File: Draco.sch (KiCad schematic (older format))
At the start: 50 parts, among them J1 Conn_01x03, J10 Conn_01x03, J11 Conn_01x06, J12 Conn_02x05_Odd_Even, J13 Conn_01x04, J14 Conn_01x01, J15 Micro_SD_Card, J2 Conn_01x03, J3 Conn_01x03, J4 Conn_01x03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

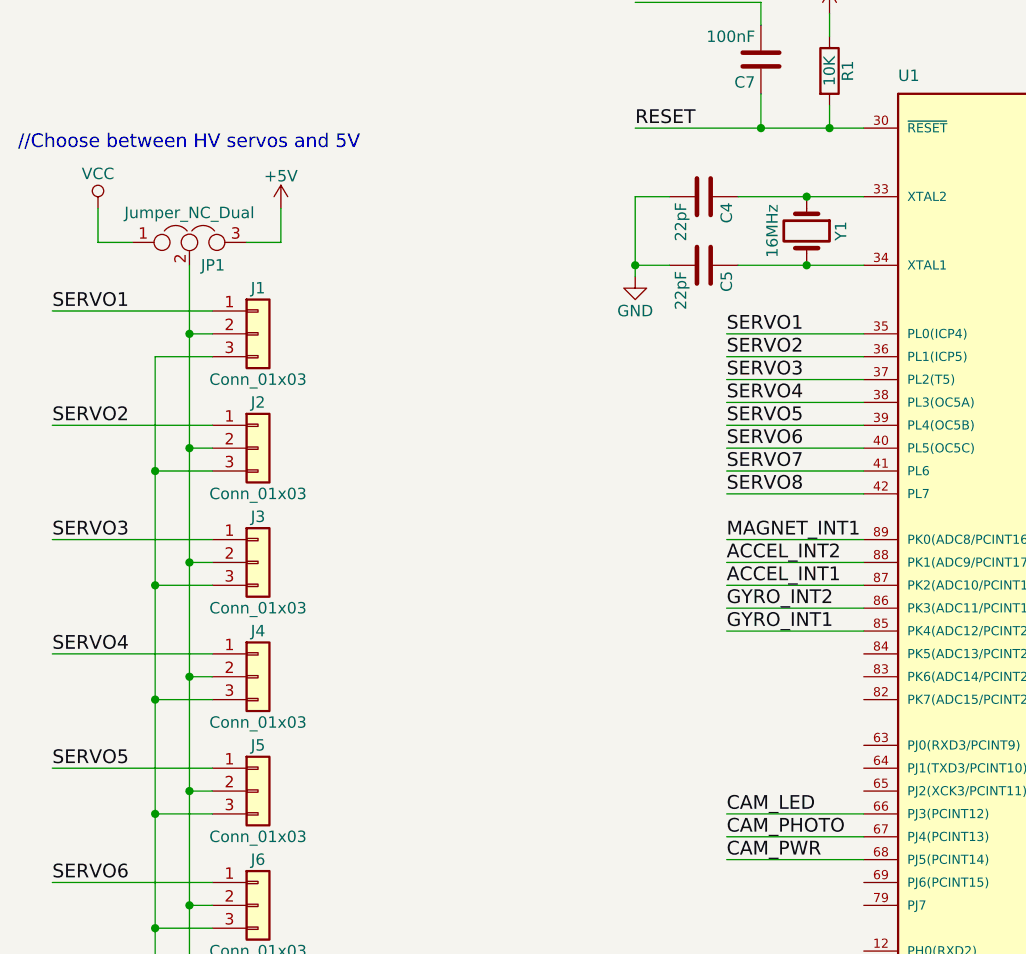
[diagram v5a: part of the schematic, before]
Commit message: moved charge module, routed lots of stuff
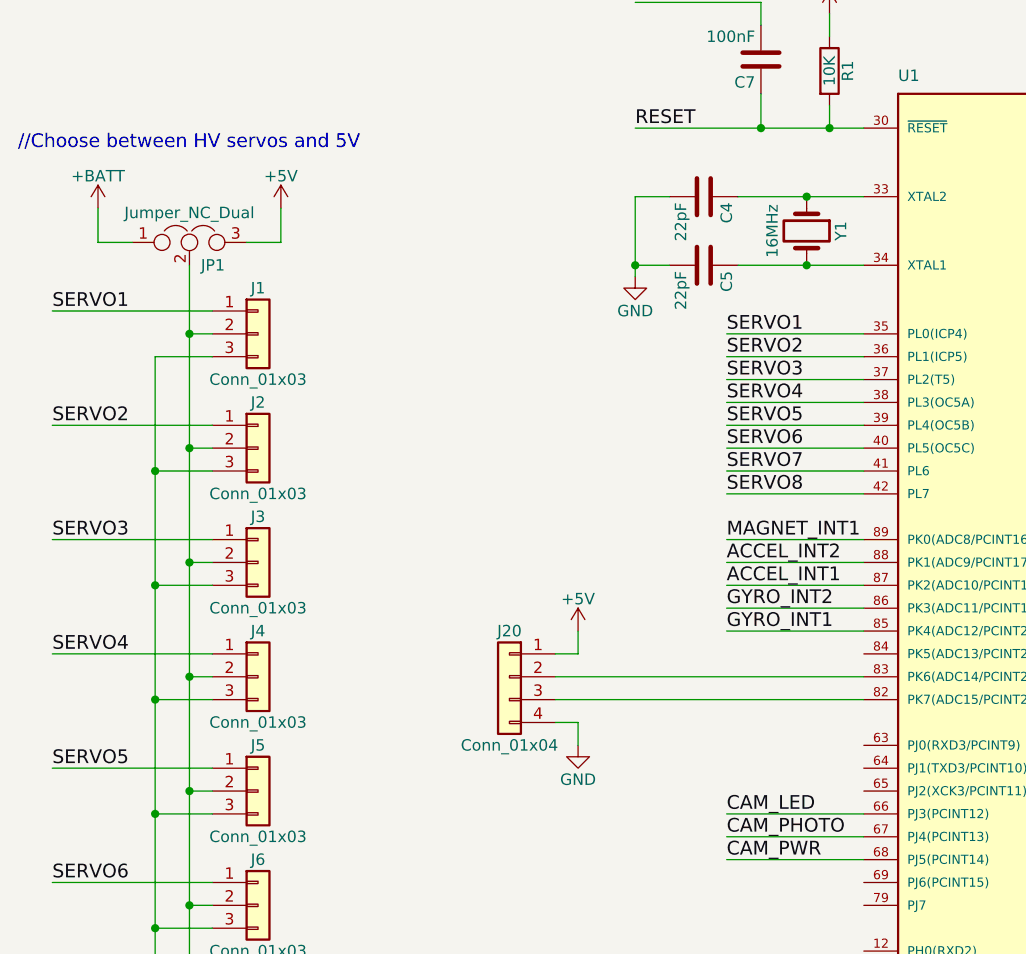
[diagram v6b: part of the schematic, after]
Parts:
- added J20: Conn_01x04, Pin_Headers:Pin_Header_Angled_1x04_Pitch2.54mm, symbol Conn_01x04
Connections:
- net VCC is gone; now on net +BATT: JP1.1
- net +5V: now also J20.1 (Pin_1)
- net GND: now also J20.4 (Pin_4)
- net at U1.82 (PK7(ADC15/PCINT23)): now also J20.3 (Pin_3)
- net at U1.83 (PK6(ADC14/PCINT22)): now also J20.2 (Pin_2)
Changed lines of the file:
@@
 LIBS:TXB0104DR
 LIBS:LOGIC-TXS0108EPWR_TSSOP20_
-LIBS:CurrentControlSystems
 LIBS:Draco-cache
 EELAYER 25 0
@@
 Text Notes 11000 4800 0    60   ~ 0
 CAM_PWR needs 9.8k-3.13k
-$Comp
-L VCC #PWR030
-U 1 1 5A686F0B
-P 1450 2550
-F 0 "#PWR030" H 1450 2400 50  0001 C CNN
-F 1 "VCC" H 1450 2700 50  0000 C CNN
-F 2 "" H 1450 2550 50  0001 C CNN
-F 3 "" H 1450 2550 50  0001 C CNN
-	1    1450 2550
-	1    0    0    -1
-$EndComp
 Wire Wire Line
 	4800 6100 4200 6100
@@
 Text Label 8050 7100 2    60   ~ 0
 VBAT2
+$Comp
+L Conn_01x04 J20
+U 1 1 5A6A227C
+P 3250 4600
+F 0 "J20" H 3250 4800 50  0000 C CNN
+F 1 "Conn_01x04" H 3250 4300 50  0000 C CNN
+F 2 "Pin_Headers:Pin_Header_Angled_1x04_Pitch2.54mm" H 3250 4600 50  0001 C CNN
+F 3 "" H 3250 4600 50  0001 C CNN
+	1    3250 4600
+	-1   0    0    -1
+$EndComp
+Wire Wire Line
+	4800 4600 3450 4600
+Wire Wire Line
+	4800 4700 3450 4700
+Wire Wire Line
+	3450 4500 3550 4500
+Wire Wire Line
+	3550 4500 3550 4400
+Wire Wire Line
+	3450 4800 3550 4800
+Wire Wire Line
+	3550 4800 3550 4900
+$Comp
+L GND #PWR034
+U 1 1 5A6A2B9C
+P 3550 4900
+F 0 "#PWR034" H 3550 4650 50  0001 C CNN
+F 1 "GND" H 3550 4750 50  0000 C CNN
+F 2 "" H 3550 4900 50  0001 C CNN
+F 3 "" H 3550 4900 50  0001 C CNN
+	1    3550 4900
+	1    0    0    -1
+$EndComp
+$Comp
+L +5V #PWR035
+U 1 1 5A6A2F82
+P 3550 4400
+F 0 "#PWR035" H 3550 4250 50  0001 C CNN
+F 1 "+5V" H 3550 4540 50  0000 C CNN
+F 2 "" H 3550 4400 50  0001 C CNN
+F 3 "" H 3550 4400 50  0001 C CNN
+	1    3550 4400
+	1    0    0    -1
+$EndComp
+$Comp
+L +BATT #PWR?
+U 1 1 5A6A6502
+P 1450 2550
+F 0 "#PWR?" H 1450 2400 50  0001 C CNN
+F 1 "+BATT" H 1450 2690 50  0000 C CNN
+F 2 "" H 1450 2550 50  0001 C CNN
+F 3 "" H 1450 2550 50  0001 C CNN
+	1    1450 2550
+	1    0    0    -1
+$EndComp
 $EndSCHEMATC

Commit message: Routed 50%
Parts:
- J20: footprint Pin_Headers:Pin_Header_Angled_1x04_Pitch2.54mm -> Connectors_JST:JST_XH_B04B-XH-A_04x2.50mm_Straight
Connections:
- net 3V_LORA_NSS: now also U2.6 (A5); no longer U2.7 (A6)
- net 3V_LORA_RST: now also U2.5 (A4); no longer U2.9 (A8)
- net 3V_MISO: now also U2.9 (A8); no longer U2.5 (A4)
- net 3V_MOSI: now also U2.8 (A7); no longer U2.4 (A3)
- net 3V_SCK: now also U2.7 (A6); no longer U2.6 (A5)
- net 3V_SD_NSS: now also U2.4 (A3); no longer U2.8 (A7)
- net 5V_LORA_NSS: now also U2.15 (B5); no longer U2.14 (B6)
- net 5V_LORA_RST: now also U2.16 (B4); no longer U2.12 (B8)
- net 5V_MISO: now also U2.12 (B8); no longer U2.16 (B4)
- net 5V_MOSI: now also U2.13 (B7); no longer U2.17 (B3)
- net 5V_SCK: now also U2.14 (B6); no longer U2.15 (B5)
- net 5V_SD_NSS: now also U2.17 (B3); no longer U2.13 (B7)
- net CAM_PHOTO: now also R10.2; no longer R11.2
- net CAM_PWR: now also R11.2; no longer R10.2
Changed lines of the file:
@@
 LIBS:TXB0104DR
 LIBS:LOGIC-TXS0108EPWR_TSSOP20_
+LIBS:CurrentControlSystems
 LIBS:Draco-cache
 EELAYER 25 0
@@
 Text Label 10900 7700 0    60   ~ 0
 3V_SDA
-Text Label 13100 7800 2    60   ~ 0
+Text Label 13100 8200 2    60   ~ 0
 5V_MOSI
-Text Label 13100 7900 2    60   ~ 0
+Text Label 13100 8300 2    60   ~ 0
 5V_MISO
+Text Label 13100 8100 2    60   ~ 0
+5V_SCK
+Text Label 10900 8200 0    60   ~ 0
+3V_MOSI
+Text Label 10900 8300 0    60   ~ 0
+3V_MISO
+Text Label 10900 8100 0    60   ~ 0
+3V_SCK
 Text Label 13100 8000 2    60   ~ 0
-5V_SCK
-Text Label 10900 7800 0    60   ~ 0
-3V_MOSI
-Text Label 10900 7900 0    60   ~ 0
-3V_MISO
+5V_LORA_NSS
 Text Label 10900 8000 0    60   ~ 0
-3V_SCK
-Text Label 13100 8100 2    60   ~ 0
-5V_LORA_NSS
-Text Label 10900 8100 0    60   ~ 0
 3V_LORA_NSS
 Text Label 13650 7650 0    60   ~ 0
@@
 Text Label 12700 4950 0    60   ~ 0
 3V_SD_NSS
-Text Label 10900 8200 0    60   ~ 0
+Text Label 10900 7800 0    60   ~ 0
 3V_SD_NSS
-Text Label 13100 8200 2    60   ~ 0
+Text Label 13100 7800 2    60   ~ 0
 5V_SD_NSS
 Text Label 8050 2900 2    60   ~ 0
@@
 Text Label 13650 8150 0    60   ~ 0
 3V_LORA_RST
-Text Label 10900 8300 0    60   ~ 0
+Text Label 10900 7900 0    60   ~ 0
 3V_LORA_RST
-Text Label 13100 8300 2    60   ~ 0
+Text Label 13100 7900 2    60   ~ 0
 5V_LORA_RST
 Text Label 8050 6200 2    60   ~ 0
@@
 	11500 7700 10900 7700
 Wire Wire Line
+	12400 8200 13100 8200
+Wire Wire Line
+	12400 8300 13100 8300
+Wire Wire Line
+	12400 8100 13100 8100
+Wire Wire Line
+	11500 8200 10900 8200
+Wire Wire Line
+	11500 8300 10900 8300
+Wire Wire Line
+	11500 8100 10900 8100
+Wire Wire Line
+	12400 8000 13100 8000
+Wire Wire Line
+	11500 8000 10900 8000
+Wire Wire Line
+	14600 7650 13650 7650
+Wire Wire Line
+	14600 7750 13650 7750
+Wire Wire Line
+	14600 7850 13650 7850
+Wire Wire Line
+	14600 7950 13650 7950
+Wire Wire Line
+	13650 2150 12950 2150
+Wire Wire Line
+	13650 2300 12950 2300
+Wire Wire Line
+	13350 5150 13800 5150
+Wire Wire Line
+	13700 5150 13700 4500
+Wire Wire Line
+	13800 5350 13700 5350
+Wire Wire Line
+	13700 5350 13700 5850
+Wire Wire Line
+	13800 5250 12700 5250
+Wire Wire Line
+	13800 5450 12700 5450
+Wire Wire Line
+	13800 5050 12700 5050
+Wire Wire Line
+	13800 4950 12700 4950
+Wire Wire Line
+	11500 7800 10900 7800
+Wire Wire Line
 	12400 7800 13100 7800
 Wire Wire Line
+	7400 2900 8050 2900
+Wire Wire Line
+	4800 3100 4200 3100
+Wire Wire Line
+	4800 3200 4200 3200
+Wire Wire Line
+	4800 3300 4200 3300
+Wire Wire Line
+	4800 3400 4200 3400
+Wire Wire Line
+	4800 3500 4200 3500
+Wire Wire Line
+	4800 3600 4200 3600
+Wire Wire Line
+	4800 3700 4200 3700
+Wire Wire Line
+	4800 3800 4200 3800
+Wire Wire Line
+	7400 6500 8050 6500
+Wire Wire Line
+	7400 6400 8050 6400
+Wire Wire Line
+	11500 7500 11400 7500
+Wire Wire Line
+	11400 7500 11400 7250
+Wire Wire Line
+	15700 7600 16200 7600
+Wire Wire Line
+	14600 8150 13650 8150
+Wire Wire Line
+	11500 7900 10900 7900
+Wire Wire Line
 	12400 7900 13100 7900
-Wire Wire Line
-	12400 8000 13100 8000
-Wire Wire Line
-	11500 7800 10900 7800
-Wire Wire Line
-	11500 7900 10900 7900
-Wire Wire Line
-	11500 8000 10900 8000
-Wire Wire Line
-	12400 8100 13100 8100
-Wire Wire Line
-	11500 8100 10900 8100
-Wire Wire Line
-	14600 7650 13650 7650
-Wire Wire Line
-	14600 7750 13650 7750
-Wire Wire Line
-	14600 7850 13650 7850
-Wire Wire Line
-	14600 7950 13650 7950
-Wire Wire Line
-	13650 2150 12950 2150
-Wire Wire Line
-	13650 2300 12950 2300
-Wire Wire Line
-	13350 5150 13800 5150
-Wire Wire Line
-	13700 5150 13700 4500
-Wire Wire Line
-	13800 5350 13700 5350
-Wire Wire Line
-	13700 5350 13700 5850
-Wire Wire Line
-	13800 5250 12700 5250
-Wire Wire Line
-	13800 5450 12700 5450
-Wire Wire Line
-	13800 5050 12700 5050
-Wire Wire Line
-	13800 4950 12700 4950
-Wire Wire Line
-	11500 8200 10900 8200
-Wire Wire Line
-	12400 8200 13100 8200
-Wire Wire Line
-	7400 2900 8050 2900
-Wire Wire Line
-	4800 3100 4200 3100
-Wire Wire Line
-	4800 3200 4200 3200
-Wire Wire Line
-	4800 3300 4200 3300
-Wire Wire Line
-	4800 3400 4200 3400
-Wire Wire Line
-	4800 3500 4200 3500
-Wire Wire Line
-	4800 3600 4200 3600
-Wire Wire Line
-	4800 3700 4200 3700
-Wire Wire Line
-	4800 3800 4200 3800
-Wire Wire Line
-	7400 6500 8050 6500
-Wire Wire Line
-	7400 6400 8050 6400
-Wire Wire Line
-	11500 7500 11400 7500
-Wire Wire Line
-	11400 7500 11400 7250
-Wire Wire Line
-	15700 7600 16200 7600
-Wire Wire Line
-	14600 8150 13650 8150
-Wire Wire Line
-	11500 8300 10900 8300
-Wire Wire Line
-	12400 8300 13100 8300
 Wire Wire Line
 	7400 6200 8050 6200
@@
 	11650 5000 11100 5000
 Wire Wire Line
+	11650 5200 11100 5200
+Wire Wire Line
 	11650 5100 11100 5100
-Wire Wire Line
-	11650 5200 11100 5200
 Wire Wire Line
 	11950 5300 11850 5300
@@
 	1    0    0    -1
 $EndComp
+Text Label 11100 5100 0    60   ~ 0
+CAM_PHOTO
 Text Label 11100 5200 0    60   ~ 0
-CAM_PHOTO
-Text Label 11100 5100 0    60   ~ 0
 CAM_PWR
 Text Label 11100 5000 0    60   ~ 0
@@
 $EndComp
 $Comp
-L GND #PWR031
+L GND #PWR030
 U 1 1 5A68BFAE
 P 9800 7950
-F 0 "#PWR031" H 9800 7700 50  0001 C CNN
+F 0 "#PWR030" H 9800 7700 50  0001 C CNN
 F 1 "GND" H 9800 7800 50  0000 C CNN
 F 2 "" H 9800 7950 50  0001 C CNN
@@
 $EndComp
 $Comp
-L +BATT #PWR032
+L +BATT #PWR031
 U 1 1 5A68C099
 P 9800 7100
-F 0 "#PWR032" H 9800 6950 50  0001 C CNN
+F 0 "#PWR031" H 9800 6950 50  0001 C CNN
 F 1 "+BATT" H 9800 7240 50  0000 C CNN
 F 2 "" H 9800 7100 50  0001 C CNN
@@
 $EndComp
 $Comp
-L GND #PWR033
+L GND #PWR032
 U 1 1 5A6DAD78
 P 8300 6050
-F 0 "#PWR033" H 8300 5800 50  0001 C CNN
+F 0 "#PWR032" H 8300 5800 50  0001 C CNN
 F 1 "GND" H 8300 5900 50  0000 C CNN
 F 2 "" H 8300 6050 50  0001 C CNN
@@
 F 0 "J20" H 3250 4800 50  0000 C CNN
 F 1 "Conn_01x04" H 3250 4300 50  0000 C CNN
-F 2 "Pin_Headers:Pin_Header_Angled_1x04_Pitch2.54mm" H 3250 4600 50  0001 C CNN
+F 2 "Connectors_JST:JST_XH_B04B-XH-A_04x2.50mm_Straight" H 3250 4600 50  0001 C CNN
 F 3 "" H 3250 4600 50  0001 C CNN
 	1    3250 4600
@@
 	3550 4800 3550 4900
 $Comp
-L GND #PWR034
+L GND #PWR033
 U 1 1 5A6A2B9C
 P 3550 4900
-F 0 "#PWR034" H 3550 4650 50  0001 C CNN
+F 0 "#PWR033" H 3550 4650 50  0001 C CNN
 F 1 "GND" H 3550 4750 50  0000 C CNN
 F 2 "" H 3550 4900 50  0001 C CNN
@@
 $EndComp
 $Comp
-L +5V #PWR035
+L +5V #PWR034
 U 1 1 5A6A2F82
 P 3550 4400
-F 0 "#PWR035" H 3550 4250 50  0001 C CNN
+F 0 "#PWR034" H 3550 4250 50  0001 C CNN
 F 1 "+5V" H 3550 4540 50  0000 C CNN
 F 2 "" H 3550 4400 50  0001 C CNN
@@
 $EndComp
 $Comp
-L +BATT #PWR?
+L +BATT #PWR035
 U 1 1 5A6A6502
 P 1450 2550
-F 0 "#PWR?" H 1450 2400 50  0001 C CNN
+F 0 "#PWR035" H 1450 2400 50  0001 C CNN
 F 1 "+BATT" H 1450 2690 50  0000 C CNN
 F 2 "" H 1450 2550 50  0001 C CNN

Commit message: Finished left side
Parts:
- removed J14: Conn_01x01, Pin_Headers:Pin_Header_Straight_1x01_Pitch2.54mm, symbol Conn_01x01
- J11: footprint Connectors_JST:JST_PH_B6B-PH-K_06x2.00mm_Straight -> Socket_Strips:Socket_Strip_Straight_1x06_Pitch2.54mm
- J13: footprint Connectors_JST:JST_PH_B4B-PH-K_04x2.00mm_Straight -> Connectors_JST:JST_XH_B04B-XH-A_04x2.50mm_Straight
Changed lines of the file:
@@
 F 0 "J11" H 7800 9450 50  0000 C CNN
 F 1 "Conn_01x06" H 7800 8750 50  0000 C CNN
-F 2 "Connectors_JST:JST_PH_B6B-PH-K_06x2.00mm_Straight" H 7800 9150 50  0001 C CNN
+F 2 "Socket_Strips:Socket_Strip_Straight_1x06_Pitch2.54mm" H 7800 9150 50  0001 C CNN
 F 3 "" H 7800 9150 50  0001 C CNN
 	1    7800 9150
@@
 	1    0    0    -1
 $EndComp
-$Comp
-L Conn_01x01 J14
-U 1 1 5A5F4C41
-P 14100 7450
-F 0 "J14" H 14100 7550 50  0000 C CNN
-F 1 "Conn_01x01" H 14100 7350 50  0000 C CNN
-F 2 "Pin_Headers:Pin_Header_Straight_1x01_Pitch2.54mm" H 14100 7450 50  0001 C CNN
-F 3 "" H 14100 7450 50  0001 C CNN
-	1    14100 7450
-	-1   0    0    1
-$EndComp
 Text Label 8050 2800 2    60   ~ 0
 5V_LORA_NSS
@@
 F 0 "J13" H 12150 5300 50  0000 C CNN
 F 1 "Conn_01x04" H 12150 4800 50  0000 C CNN
-F 2 "Connectors_JST:JST_PH_B4B-PH-K_04x2.00mm_Straight" H 12150 5100 50  0001 C CNN
+F 2 "Connectors_JST:JST_XH_B04B-XH-A_04x2.50mm_Straight" H 12150 5100 50  0001 C CNN
 F 3 "" H 12150 5100 50  0001 C CNN
 	1    12150 5100
@@
 	14500 7350 14500 8500
 Connection ~ 15050 8500
-Wire Wire Line
-	14300 7450 14600 7450
-Wire Wire Line
-	14400 7450 14400 7350
-Connection ~ 14400 7450
 Wire Wire Line
 	7400 2400 8050 2400
@@
 	1    0    0    -1
 $EndComp
+Wire Wire Line
+	14600 7450 14400 7450
+Wire Wire Line
+	14400 7450 14400 7350
 $EndSCHEMATC
